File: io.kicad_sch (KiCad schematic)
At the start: 27 parts, among them CN2 20021521-00010T1LF, J7 U.FL, J8 Conn_01x04, SW4 SW_Push, U10 nRF52833_QDxx, X1 X201632MOB4SI

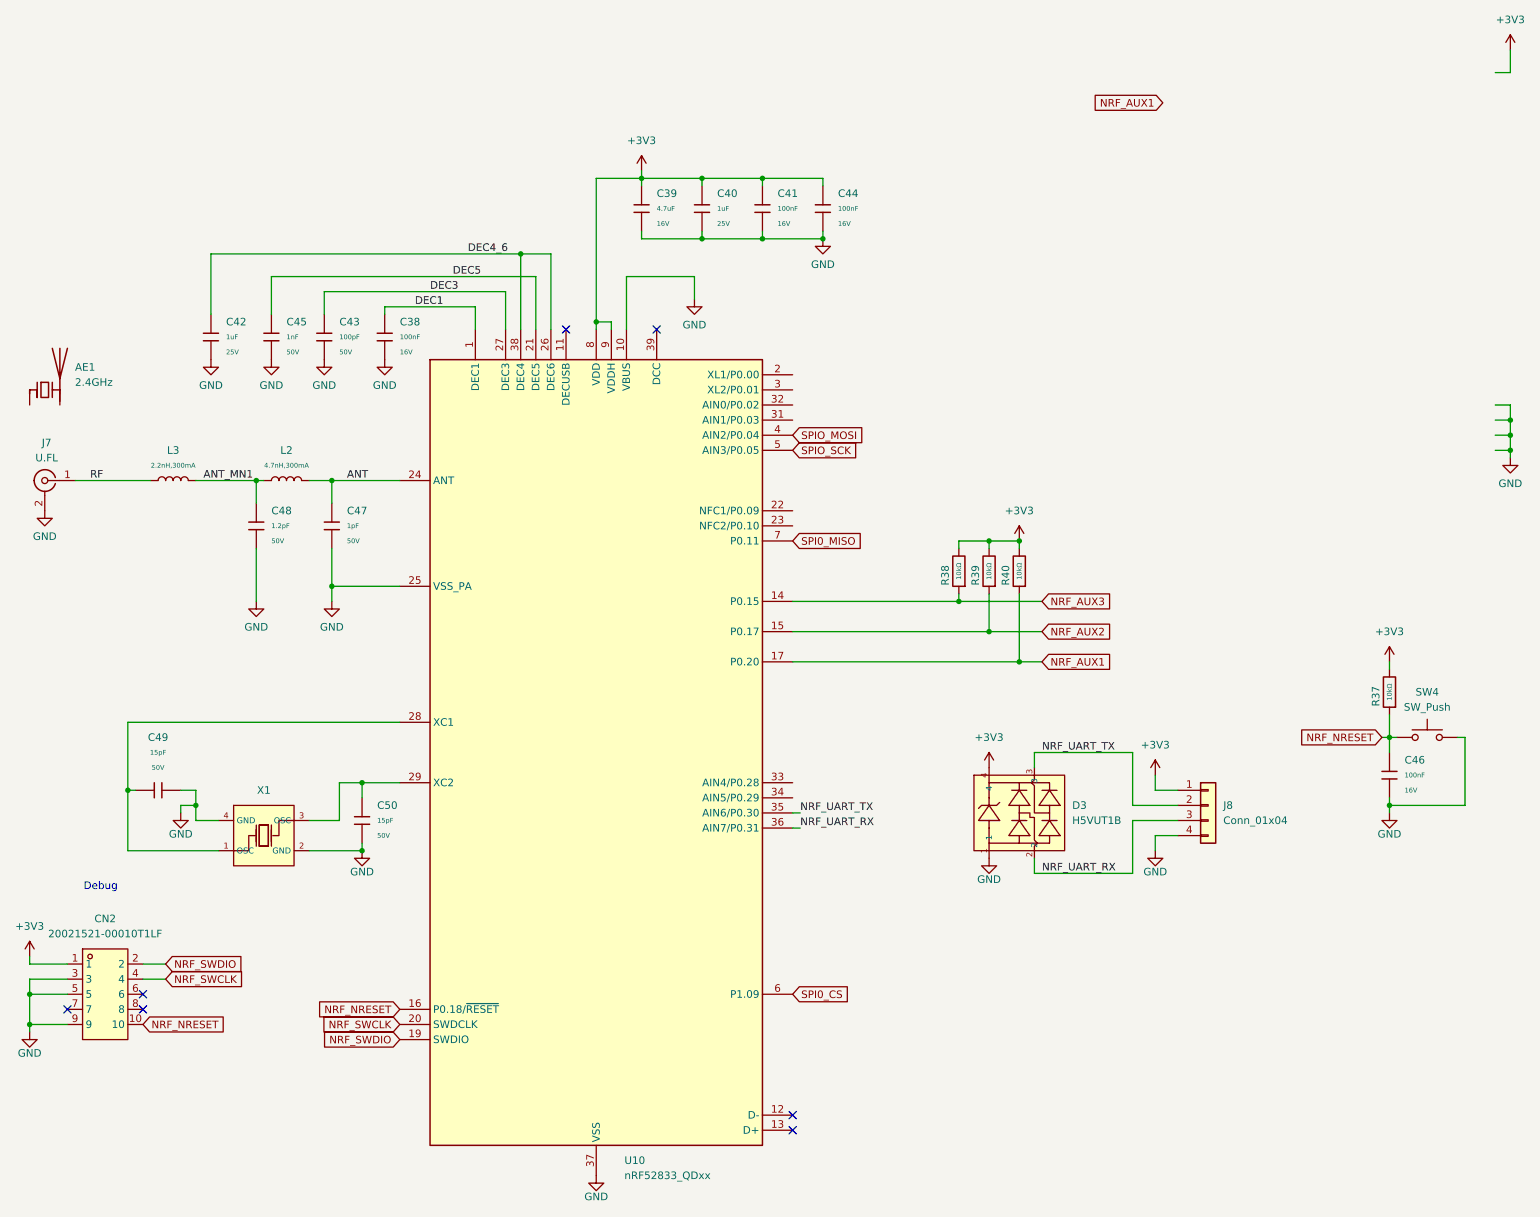
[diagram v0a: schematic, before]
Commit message: nrf54L BLE module
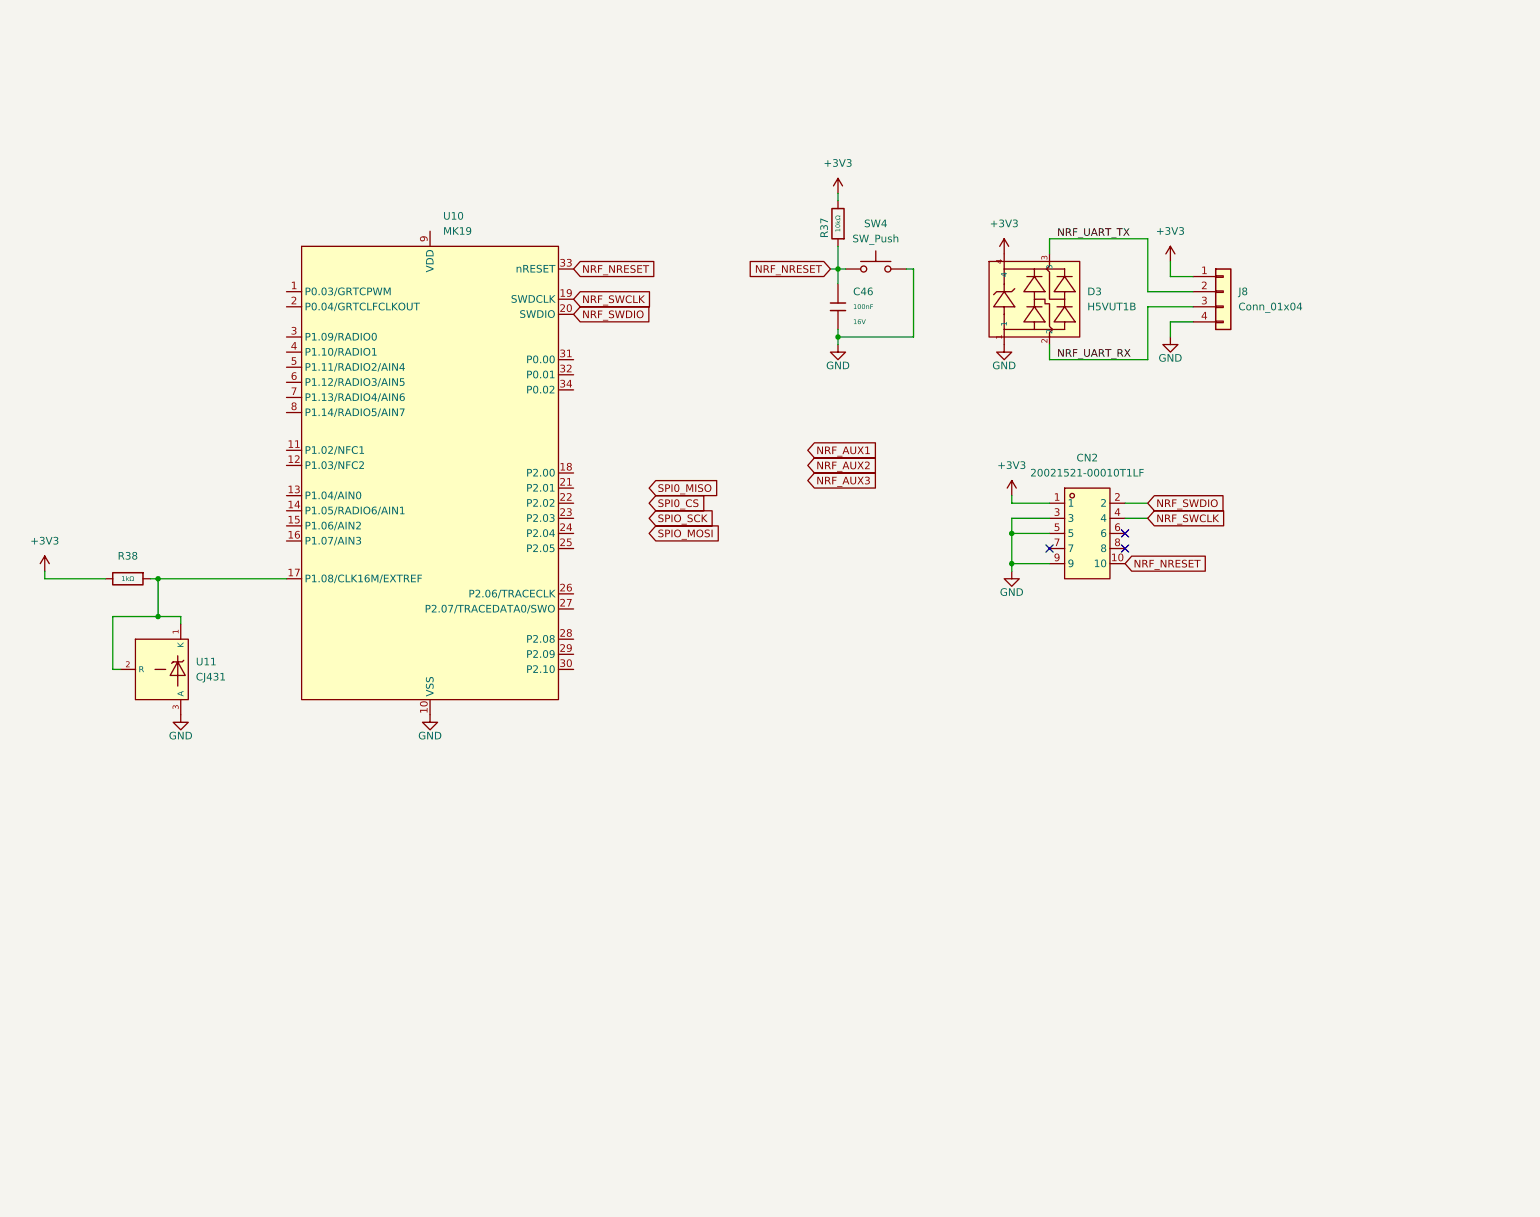
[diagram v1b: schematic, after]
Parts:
- removed AE1: 2.4GHz, PCM_JLCPCB:L_1206, symbol Device:Antenna_Chip
- removed C38, C41, C44: 100nF, PCM_JLCPCB:C_0402, symbol JLCPCB-Capacitors:0402,100nF
- removed C39: 4.7uF, PCM_JLCPCB:C_0603, symbol JLCPCB-Capacitors:0603,4.7uF
- removed C40, C42: 1uF, PCM_JLCPCB:C_0402, symbol JLCPCB-Capacitors:0402,1uF
- removed C43: 100pF, PCM_JLCPCB:C_0402, symbol JLCPCB-Capacitors:0402,100pF
- removed C45: 1nF, PCM_JLCPCB:C_0402, symbol JLCPCB-Capacitors:0402,1nF
- removed C47: 1pF, PCM_JLCPCB:C_0402, symbol JLCPCB-Capacitors:0402,1pF
- removed C48: 1.2pF, PCM_JLCPCB:C_0402, symbol JLCPCB-Capacitors:0402,1pF
- removed C49, C50: 15pF, PCM_JLCPCB:C_0402, symbol JLCPCB-Capacitors:0402,15pF
- removed J7: U.FL, PCM_JLCPCB:IPEX-SMD_BWIPX-1-001E, symbol JLCPCB-Extended:RF, Connector, U.FL
- removed L2: 4.7nH,300mA, PCM_JLCPCB:L_0402, symbol JLCPCB-Inductors:3.9nH,300mA
- removed L3: 2.2nH,300mA, PCM_JLCPCB:L_0402, symbol JLCPCB-Inductors:3.9nH,300mA
- removed R38, R39, R40: 10kΩ, PCM_JLCPCB:R_0402, symbol JLCPCB-Resistors:0402,10kΩ
- removed U10: nRF52833_QDxx, Package_DFN_QFN:QFN-40-1EP_5x5mm_P0.4mm_EP3.6x3.6mm, symbol MCU_Nordic:nRF52833_QDxx
- removed X1: X201632MOB4SI, PCM_JLCPCB:OSC-SMD_4P-L3.2-W2.5-BL, symbol JLCPCB-Crystals:Crystal, 16MHz, 9pF
- added R38: 1kΩ, PCM_JLCPCB:R_0402, symbol JLCPCB-Resistors:0402,1kΩ
- added U10: MK19, RF_Module:MokoSmart MK19, symbol RF_Module:NRF54L15-MOKO-MK19
- added U11: CJ431, PCM_JLCPCB:SOT-23-3_L2.9-W1.6-P1.90-LS2.8-BR, symbol JLCPCB-Power:Ref, 2-36V, 100mA, CJ431
- CN2: footprint easyeda2kicad:IDC-SMD_10P-P1.27_X1270WVS-2X05B-6TV01 -> DigiKey:CONN_3220-10-0100-00_CNC
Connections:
- net +3V3: now also R38.2
- net GND: now also U10.10 (VSS), U11.3 (A)
- net NRF_NRESET: now also U10.33 (nRESET)
- net NRF_SWCLK: now also U10.19 (SWDCLK)
- net NRF_SWDIO: now also U10.20 (SWDIO)
- new net: R38.1, U10.17 (P1.08/CLK16M/EXTREF), U11.1 (K), U11.2 (R)
- no-connect marks 7 -> 3
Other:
- note removed: "Debug"
- moved on the sheet: C46, D3, J8, R37, SW4
